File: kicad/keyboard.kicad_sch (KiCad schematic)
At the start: 64 parts

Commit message: Cleaner schematic: matrix grid + grouped sections
Rewrite gen_schematic.py to organize the schematic like a real keyboard design:
- Switch Matrix drawn as a grid (switch + series diode per cell) with COL
  labels on top and ROW labels on the left
- Separate labelled sections for Microcontroller, Encoder, and Power
  (battery / power switch / reset)
- Fix encoder pin mapping (RotaryEncoder_Switch uses A/B/C/S1/S2 names) and
  render the encoder push-switch diode (D30, ENC1_SW -> P11)
All critical nets verified present; ERC violations down from 142 to ~21.
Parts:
- D1, D10, D11, D12, D13, D14, D15, D16, D17, D18, D19, D2, D20, D21, D22, D23, D24, D25, D26, D27, D28, D29, D3, D30, D4, D5, D6, D7, D8, D9: footprint ceoloide:diode_tht_sod123 -> (none)
- ENC1: value RotaryEncoder_Switch -> EVQWGD001; footprint ceoloide:encoder_evqwgd001 -> (none)
- JST1: value Conn_01x02_Pin -> Battery; footprint ceoloide:battery_connector_jst_ph_2 -> (none)
- MCU1: value Conn_02x12_Odd_Even -> nice!nano; footprint ceoloide:mcu_nice_nano -> (none)
- PWR1: value SW_SPDT -> Power SW; footprint ceoloide:power_switch_smd_side -> (none)
- RST1: value SW_Push -> Reset; footprint ceoloide:reset_switch_tht_top -> (none)
- S1, S10, S11, S12, S13, S14, S15, S16, S17, S18, S19, S2, S20, S21, S22, S23, S24, S25, S26, S27, S28, S29, S3, S4, S5, S6, S7, S8, S9: footprint ceoloide:switch_choc_v1_v2 -> (none)
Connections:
- net P11 is gone; now on net ENC1_SW: D12.2 (A), D16.2 (A), D20.2 (A), D24.2 (A), D30.2 (A), D4.2 (A), D8.2 (A), MCU1.10 (Pin_10)
- net P12 is gone; now on net ENC1_SW: D11.2 (A), D15.2 (A), D19.2 (A), D23.2 (A), D3.2 (A), D7.2 (A), MCU1.9 (Pin_9)
- net P14 is gone; now on net ENC1_SW: D1.2 (A), D13.2 (A), D17.2 (A), D21.2 (A), D5.2 (A), D9.2 (A), MCU1.15 (Pin_15)
- net P16 is gone; now on net ENC1_SW: MCU1.14 (Pin_14), S21.1, S22.1, S23.1, S24.1, S26.1
- net P17 is gone; now on net ENC1_SW: MCU1.7 (Pin_7), S17.1, S18.1, S19.1, S20.1, S27.1
- net P18 is gone; now on net ENC1_SW: MCU1.17 (Pin_17), S13.1, S14.1, S15.1, S16.1, S28.1
- net P19 is gone; now on net ENC1_SW: MCU1.18 (Pin_18), S10.1, S11.1, S12.1, S29.1, S9.1
- net P20 is gone; now on net ENC1_SW: MCU1.19 (Pin_19), S5.1, S6.1, S7.1, S8.1
- net P21 is gone; now on net ENC1_SW: MCU1.20 (Pin_20), S1.1, S2.1, S3.1, S4.1
- net index_bottom is gone; now on net ENC1_SW: D17.1 (K), S17.2
- net index_home is gone; now on net ENC1_SW: D18.1 (K), S18.2
- net index_num is gone; now on net ENC1_SW: D20.1 (K), S20.2
- net index_top is gone; now on net ENC1_SW: D19.1 (K), S19.2
- net inner_bottom is gone; now on net ENC1_SW: D21.1 (K), S21.2
- net inner_home is gone; now on net ENC1_SW: D22.1 (K), S22.2
- net inner_num is gone; now on net ENC1_SW: D24.1 (K), S24.2
- net inner_top is gone; now on net ENC1_SW: D23.1 (K), S23.2
- net middle_bottom is gone; now on net ENC1_SW: D13.1 (K), S13.2
- net middle_home is gone; now on net ENC1_SW: D14.1 (K), S14.2
- net middle_num is gone; now on net ENC1_SW: D16.1 (K), S16.2
- net middle_top is gone; now on net ENC1_SW: D15.1 (K), S15.2
- net outer_bottom is gone; now on net ENC1_SW: D1.1 (K), S1.2
- net outer_home is gone; now on net ENC1_SW: D2.1 (K), S2.2
- net outer_num is gone; now on net ENC1_SW: D4.1 (K), S4.2
- net outer_top is gone; now on net ENC1_SW: D3.1 (K), S3.2
- net pinky_bottom is gone; now on net ENC1_SW: D5.1 (K), S5.2
- net pinky_home is gone; now on net ENC1_SW: D6.1 (K), S6.2
- net pinky_num is gone; now on net ENC1_SW: D8.1 (K), S8.2
- net pinky_top is gone; now on net ENC1_SW: D7.1 (K), S7.2
- net ring_bottom is gone; now on net ENC1_SW: D9.1 (K), S9.2
- net ring_home is gone; now on net ENC1_SW: D10.1 (K), S10.2
- net ring_num is gone; now on net ENC1_SW: D12.1 (K), S12.2
- net ring_top is gone; now on net ENC1_SW: D11.1 (K), S11.2
- net ENC1_A: now also ENC1.A
- net ENC1_C: now also ENC1.C
- net ENC1_SW: now also D10.2 (A), D14.2 (A), D18.2 (A), D2.2 (A), D22.2 (A), D25.1 (K), D26.2 (A), D27.2 (A), D28.2 (A), D29.2 (A), D6.2 (A), ENC1.S2, MCU1.8 (Pin_8), S26.2, S27.2, S28.2, S29.2
- net GND: now also ENC1.B
- net P15: now also D25.2 (A), ENC1.S1, S25.2
- net P2: now also D26.1 (K), D27.1 (K), D28.1 (K), D29.1 (K); no longer D26.2 (A), D27.2 (A), D28.2 (A), D29.2 (A)
- removed net P13: D10.2 (A), D14.2 (A), D18.2 (A), D2.2 (A), D22.2 (A), D25.2 (A), D6.2 (A), MCU1.8 (Pin_8)
- removed net home_cluster: D27.1 (K), S27.2
- removed net inner_cluster: D26.1 (K), S26.2
- removed net oouter_cluster: D29.1 (K), S29.2
- removed net outer_cluster: D28.1 (K), S28.2
- removed net single_home: D25.1 (K), S25.2
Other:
- note added: "Encoder"
- note added: "Microcontroller"
- note added: "Power"
- note added: "Switch Matrix"

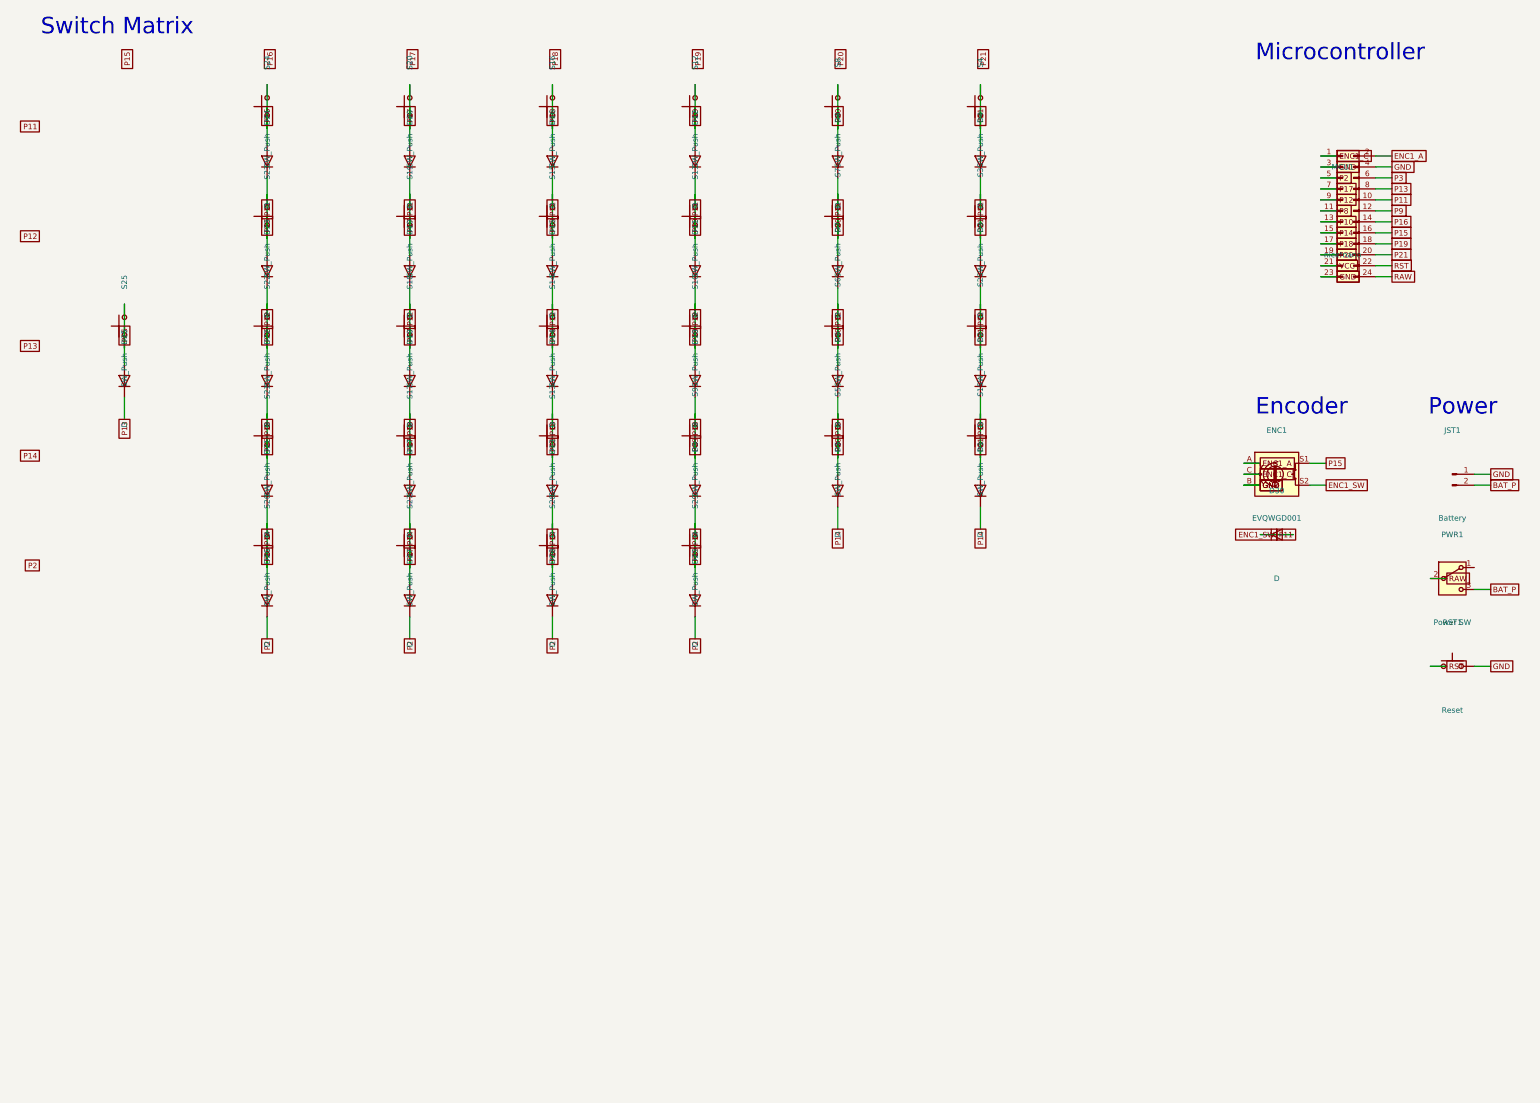
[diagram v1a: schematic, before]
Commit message: Match Lily58 schematic styling: boxed sections + matrix grid
- Wrap each subsystem in a titled section box with a descriptive annotation
  (Switch Matrix, Microcontroller, Encoder, Power/Reset), like the Lily58
  reference schematic
- Draw the switch matrix as a grid of vertical switch->diode cells with COL
  tags on top and ROW tags on the left
- Add box/note/hlabel helpers and multi-line annotations
- Fix a connectivity bug where the P11 row diodes + encoder push-switch diode
  (D30) shorted onto ENC1_SW; render D30 vertically so its labels separate.
  Netlist now fully correct (P11 = 6 matrix diodes + D30 + MCU; ENC1_SW
  isolated). ERC violations 142 -> 18 (all cosmetic single-pin labels).
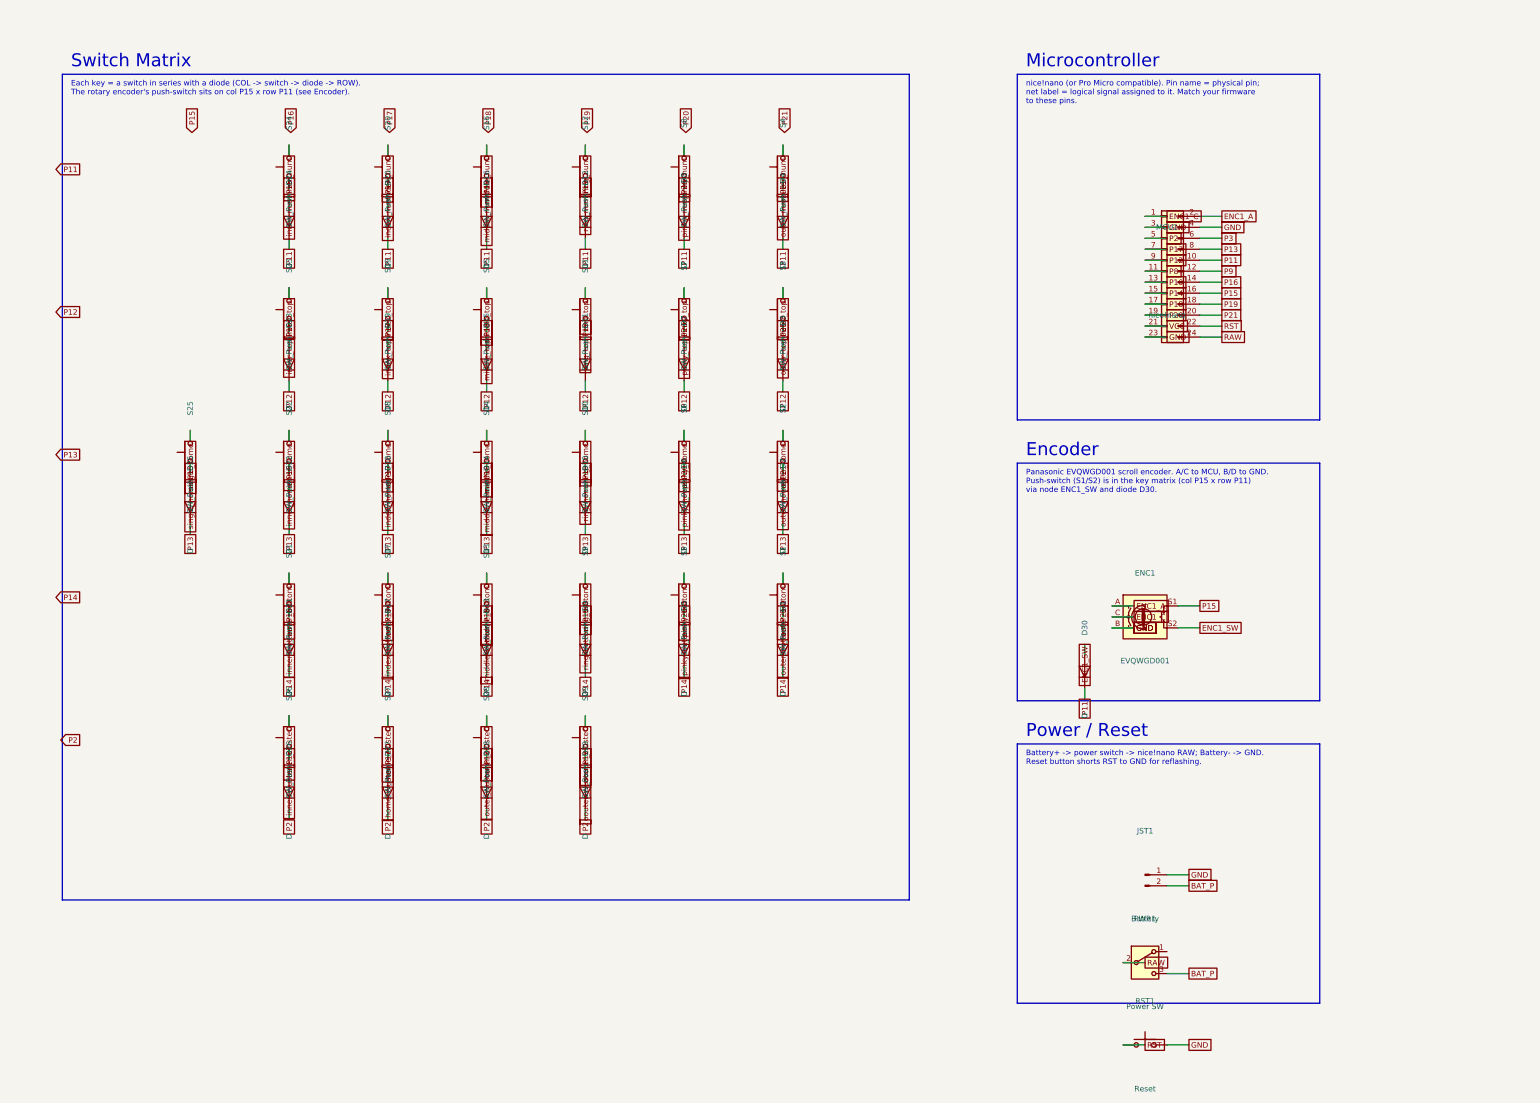
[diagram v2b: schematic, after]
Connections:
- net ENC1_SW: no longer D1.1 (K), D1.2 (A), D10.1 (K), D10.2 (A), D11.1 (K), D11.2 (A), D12.1 (K), D12.2 (A), D13.1 (K), D13.2 (A), D14.1 (K), D14.2 (A), D15.1 (K), D15.2 (A), D16.1 (K), D16.2 (A), D17.1 (K), D17.2 (A), D18.1 (K), D18.2 (A), D19.1 (K), D19.2 (A), D2.1 (K), D2.2 (A), D20.1 (K), D20.2 (A), D21.1 (K), D21.2 (A), D22.1 (K), D22.2 (A), D23.1 (K), D23.2 (A), D24.1 (K), D24.2 (A), D25.1 (K), D26.2 (A), D27.2 (A), D28.2 (A), D29.2 (A), D3.1 (K), D3.2 (A), D30.1 (K), D4.1 (K), D4.2 (A), D5.1 (K), D5.2 (A), D6.1 (K), D6.2 (A), D7.1 (K), D7.2 (A), D8.1 (K), D8.2 (A), D9.1 (K), D9.2 (A), MCU1.10 (Pin_10), MCU1.14 (Pin_14), MCU1.15 (Pin_15), MCU1.17 (Pin_17), MCU1.18 (Pin_18), MCU1.19 (Pin_19), MCU1.20 (Pin_20), MCU1.7 (Pin_7), MCU1.8 (Pin_8), MCU1.9 (Pin_9), S1.1, S1.2, S10.1, S10.2, S11.1, S11.2, S12.1, S12.2, S13.1, S13.2, S14.1, S14.2, S15.1, S15.2, S16.1, S16.2, S17.1, S17.2, S18.1, S18.2, S19.1, S19.2, S2.1, S2.2, S20.1, S20.2, S21.1, S21.2, S22.1, S22.2, S23.1, S23.2, S24.1, S24.2, S26.1, S26.2, S27.1, S27.2, S28.1, S28.2, S29.1, S29.2, S3.1, S3.2, S4.1, S4.2, S5.1, S5.2, S6.1, S6.2, S7.1, S7.2, S8.1, S8.2, S9.1, S9.2
- net P15: no longer D25.2 (A), S25.2
- new net P11: D12.1 (K), D16.1 (K), D20.1 (K), D24.1 (K), D30.1 (K), D4.1 (K), D8.1 (K), MCU1.10 (Pin_10)
- new net P12: D11.1 (K), D15.1 (K), D19.1 (K), D23.1 (K), D3.1 (K), D7.1 (K), MCU1.9 (Pin_9)
- new net P13: D10.1 (K), D14.1 (K), D18.1 (K), D2.1 (K), D22.1 (K), D25.1 (K), D6.1 (K), MCU1.8 (Pin_8)
- new net P14: D1.1 (K), D13.1 (K), D17.1 (K), D21.1 (K), D5.1 (K), D9.1 (K), MCU1.15 (Pin_15)
- new net P16: MCU1.14 (Pin_14), S21.1, S22.1, S23.1, S24.1, S26.1
- new net P17: MCU1.7 (Pin_7), S17.1, S18.1, S19.1, S20.1, S27.1
- new net P18: MCU1.17 (Pin_17), S13.1, S14.1, S15.1, S16.1, S28.1
- new net P19: MCU1.18 (Pin_18), S10.1, S11.1, S12.1, S29.1, S9.1
- new net P20: MCU1.19 (Pin_19), S5.1, S6.1, S7.1, S8.1
- new net P21: MCU1.20 (Pin_20), S1.1, S2.1, S3.1, S4.1
- new net home_cluster: D27.2 (A), S27.2
- new net index_bottom: D17.2 (A), S17.2
- new net index_home: D18.2 (A), S18.2
- new net index_num: D20.2 (A), S20.2
- new net index_top: D19.2 (A), S19.2
- new net inner_bottom: D21.2 (A), S21.2
- new net inner_cluster: D26.2 (A), S26.2
- new net inner_home: D22.2 (A), S22.2
- new net inner_num: D24.2 (A), S24.2
- new net inner_top: D23.2 (A), S23.2
- new net middle_bottom: D13.2 (A), S13.2
- new net middle_home: D14.2 (A), S14.2
- new net middle_num: D16.2 (A), S16.2
- new net middle_top: D15.2 (A), S15.2
- new net oouter_cluster: D29.2 (A), S29.2
- new net outer_bottom: D1.2 (A), S1.2
- new net outer_cluster: D28.2 (A), S28.2
- new net outer_home: D2.2 (A), S2.2
- new net outer_num: D4.2 (A), S4.2
- new net outer_top: D3.2 (A), S3.2
- new net pinky_bottom: D5.2 (A), S5.2
- new net pinky_home: D6.2 (A), S6.2
- new net pinky_num: D8.2 (A), S8.2
- new net pinky_top: D7.2 (A), S7.2
- new net ring_bottom: D9.2 (A), S9.2
- new net ring_home: D10.2 (A), S10.2
- new net ring_num: D12.2 (A), S12.2
- new net ring_top: D11.2 (A), S11.2
- new net single_home: D25.2 (A), S25.2
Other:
- note added: "Battery+ -> power switch -> nice!nano RAW; Battery- -> GND. Reset button shorts RST to GND for reflashing."
- note added: "Each key = a switch in series with a diode (COL -> switch -> diode -> ROW). The rotary encoder's push-switch sits on col P15 x row P11 (see Encoder)."
- note added: "Panasonic EVQWGD001 scroll encoder. A/C to MCU, B/D to GND. Push-switch (S1/S2) is in the key matrix (col P15 x row P11) via node ENC1_SW and diode D30."
- note added: "Power / Reset"
- note added: "nice!nano (or Pro Micro compatible). Pin name = physical pin; net label = logical signal assigned to it. Match your firmware to these pins."
- note removed: "Power"
